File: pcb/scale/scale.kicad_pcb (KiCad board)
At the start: 2 copper layers, 100 x 47.9 mm, 89 parts, among them J1 USB_C_Receptacle_USB2.0, J2 Conn_01x07, J3 Conn_01x04, SW1 SW_Push, SW10 SW_Push, SW11 SW_Push, SW12 SW_Push, SW13 SW_Push, SW14 SW_Push, SW15 SW_Push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

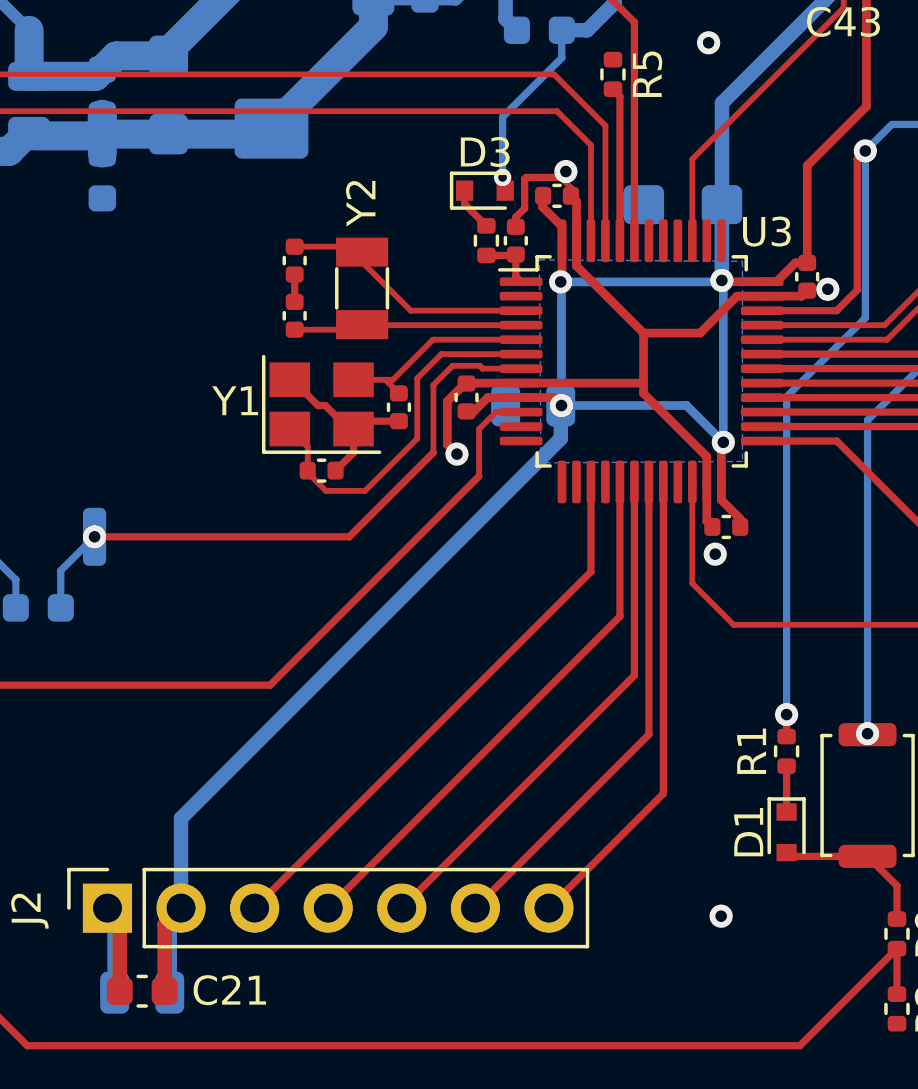
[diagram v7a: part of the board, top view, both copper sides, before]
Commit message: 电池电压检测
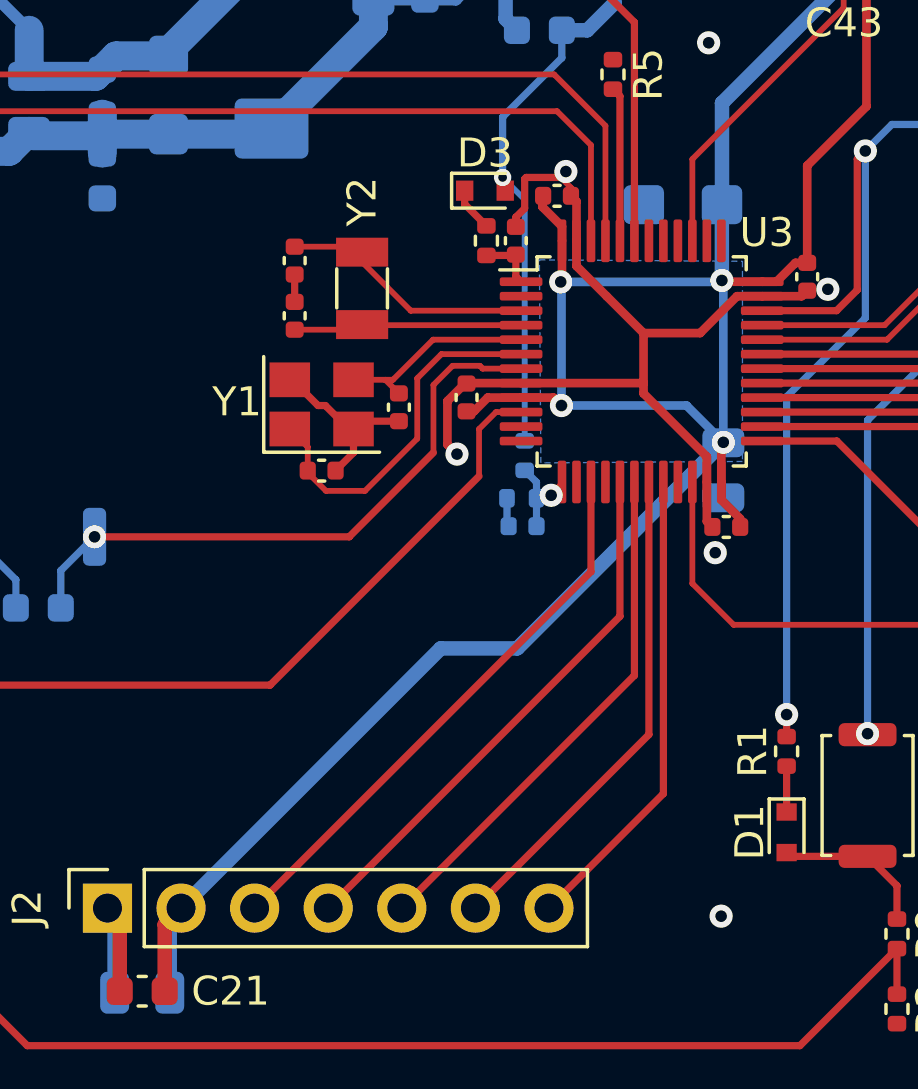
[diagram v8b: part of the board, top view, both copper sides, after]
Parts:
- added C45: 100n, Capacitor_SMD:C_0402_1005Metric, B.Cu at (107.5, 75.8)
- added R10: 1M, Resistor_SMD:R_0402_1005Metric, B.Cu at (107.5, 74.8)
- added R8: 1M, Resistor_SMD:R_0402_1005Metric, B.Cu at (107.6, 73.4)
- moved C20 6.93 mm to (114.5, 73.9), turned to -90 degrees
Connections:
- U3 pad 13: unconnected-(U3-Pad13) -> /AD_BAT
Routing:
- net +BATT: track 102.5 -> 112.4 mm
- net /AD_BAT: track 0.00 -> 3.26 mm, vias 0 -> 1
- net +3V3: track 101.5 -> 104.1 mm
- net GND: track 173.2 -> 174.2 mm
